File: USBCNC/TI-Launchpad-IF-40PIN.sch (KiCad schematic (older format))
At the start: 4 parts

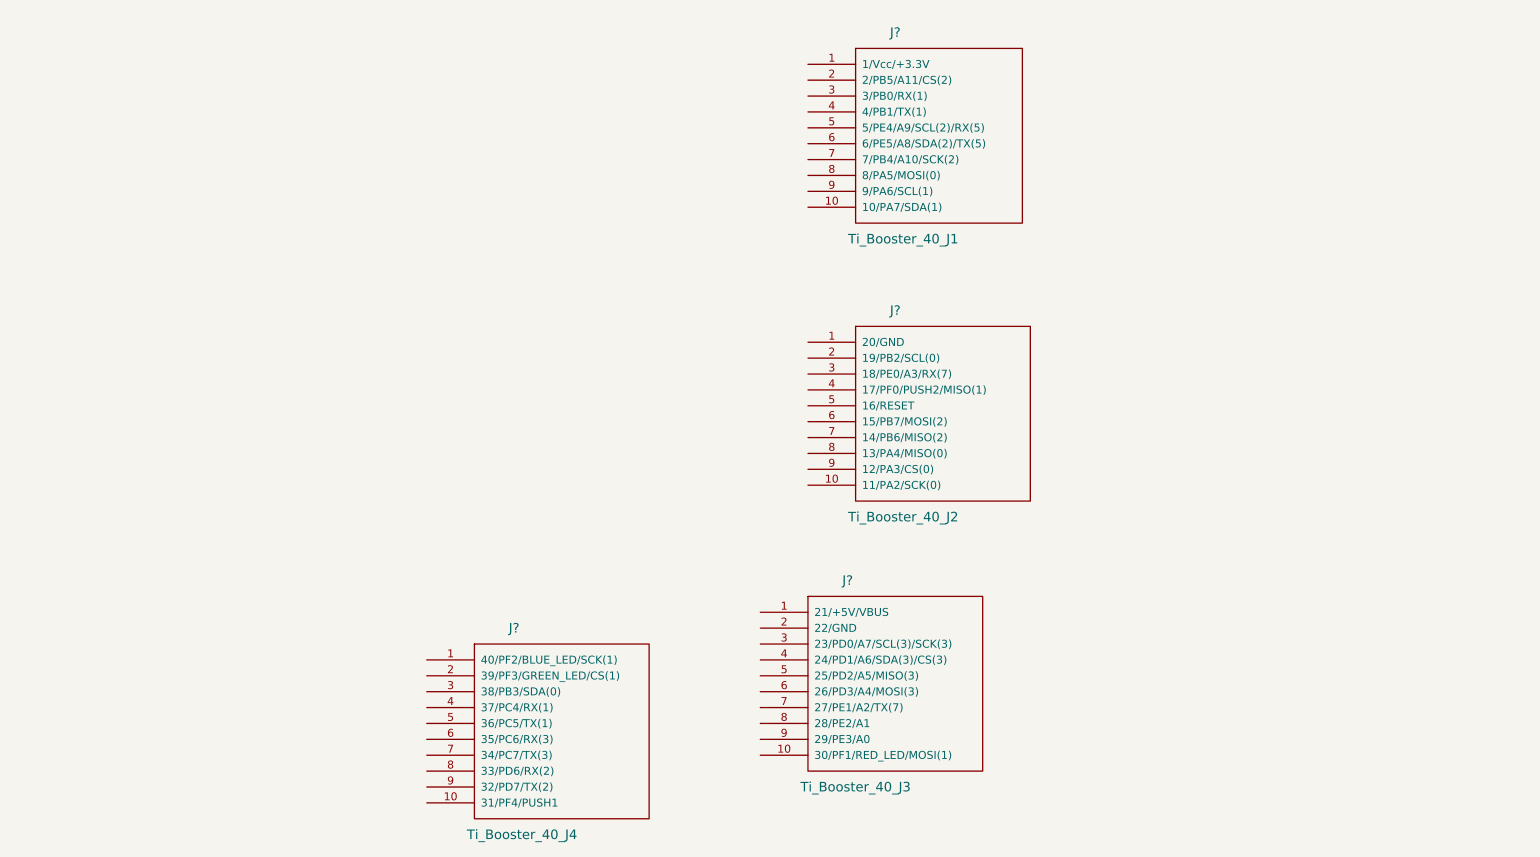
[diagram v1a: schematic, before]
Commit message: Specify global conections for the launchpad
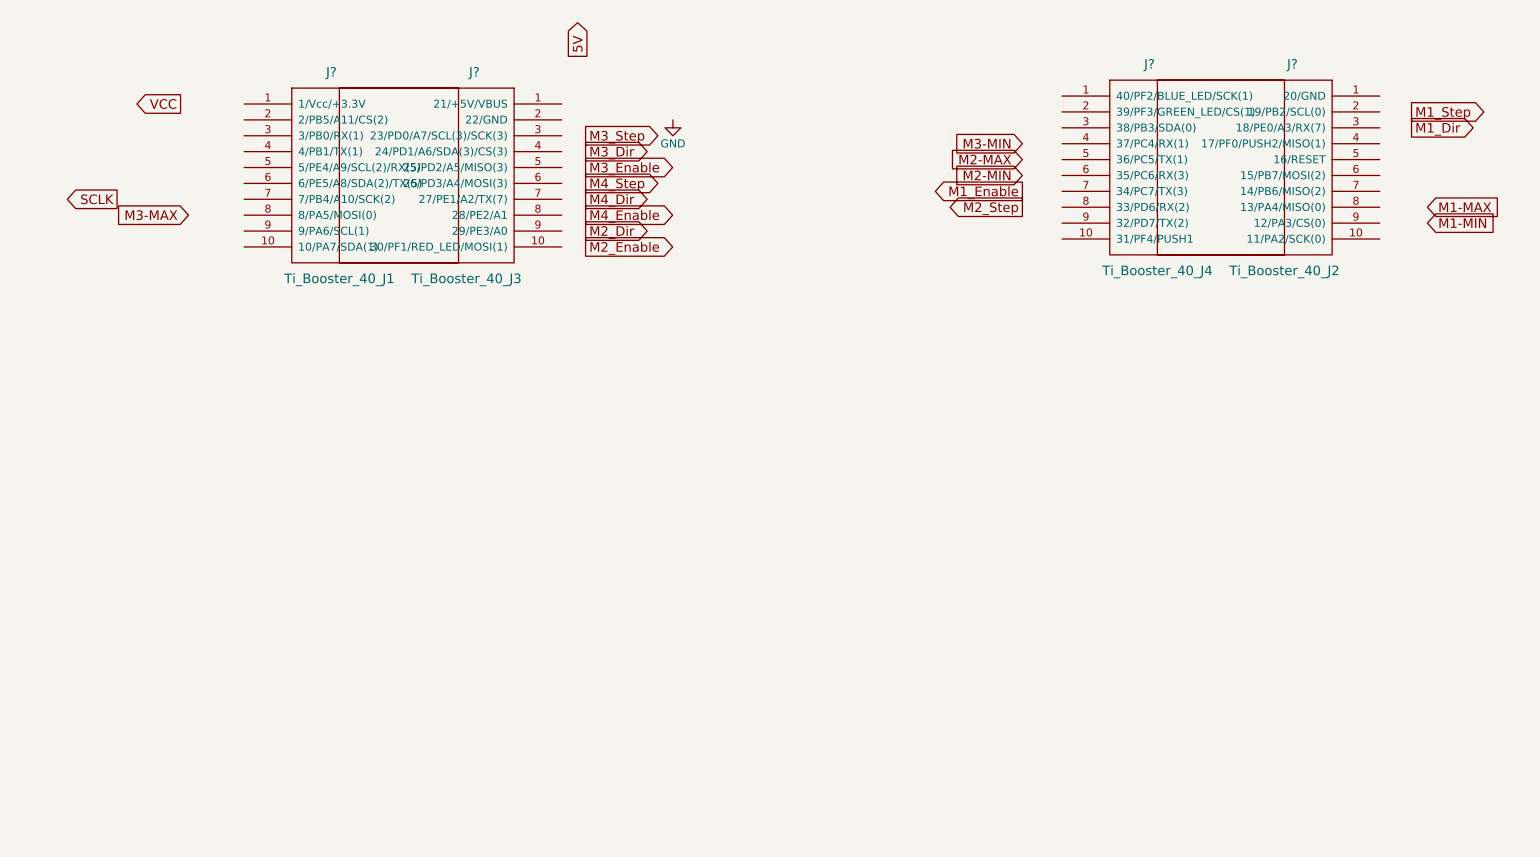
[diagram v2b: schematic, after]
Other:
- moved on the sheet: J?
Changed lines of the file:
@@
 L Ti_Booster_40_J1 J?
 U 1 1 559E3E8F
-P 6000 2500
-F 0 "J?" H 5950 3150 60  0000 C CNN
-F 1 "Ti_Booster_40_J1" H 6000 1850 60  0000 C CNN
-F 2 "" H 6000 2500 60  0000 C CNN
-F 3 "" H 6000 2500 60  0000 C CNN
-	1    6000 2500
+P 2450 2750
+F 0 "J?" H 2400 3400 60  0000 C CNN
+F 1 "Ti_Booster_40_J1" H 2450 2100 60  0000 C CNN
+F 2 "" H 2450 2750 60  0000 C CNN
+F 3 "" H 2450 2750 60  0000 C CNN
+	1    2450 2750
 	1    0    0    -1
 $EndComp
@@
 L Ti_Booster_40_J2 J?
 U 1 1 559E3EEE
-P 6000 4250
-F 0 "J?" H 5950 4900 60  0000 C CNN
-F 1 "Ti_Booster_40_J2" H 6000 3600 60  0000 C CNN
-F 2 "" H 6000 4250 60  0000 C CNN
-F 3 "" H 6000 4250 60  0000 C CNN
-	1    6000 4250
-	1    0    0    -1
+P 8400 2700
+F 0 "J?" H 8350 3350 60  0000 C CNN
+F 1 "Ti_Booster_40_J2" H 8400 2050 60  0000 C CNN
+F 2 "" H 8400 2700 60  0000 C CNN
+F 3 "" H 8400 2700 60  0000 C CNN
+	1    8400 2700
+	-1   0    0    -1
 $EndComp
 $Comp
 L Ti_Booster_40_J3 J?
 U 1 1 559E3F8D
-P 5700 5950
-F 0 "J?" H 5650 6600 60  0000 C CNN
-F 1 "Ti_Booster_40_J3" H 5700 5300 60  0000 C CNN
-F 2 "" H 5700 5950 60  0000 C CNN
-F 3 "" H 5700 5950 60  0000 C CNN
-	1    5700 5950
-	1    0    0    -1
+P 3250 2750
+F 0 "J?" H 3200 3400 60  0000 C CNN
+F 1 "Ti_Booster_40_J3" H 3250 2100 60  0000 C CNN
+F 2 "" H 3250 2750 60  0000 C CNN
+F 3 "" H 3250 2750 60  0000 C CNN
+	1    3250 2750
+	-1   0    0    -1
 $EndComp
 $Comp
 L Ti_Booster_40_J4 J?
 U 1 1 559E403A
-P 3600 6250
-F 0 "J?" H 3550 6900 60  0000 C CNN
-F 1 "Ti_Booster_40_J4" H 3600 5600 60  0000 C CNN
-F 2 "" H 3600 6250 60  0000 C CNN
-F 3 "" H 3600 6250 60  0000 C CNN
-	1    3600 6250
+P 7600 2700
+F 0 "J?" H 7550 3350 60  0000 C CNN
+F 1 "Ti_Booster_40_J4" H 7600 2050 60  0000 C CNN
+F 2 "" H 7600 2700 60  0000 C CNN
+F 3 "" H 7600 2700 60  0000 C CNN
+	1    7600 2700
 	1    0    0    -1
 $EndComp
+Text GLabel 1450 2300 0    60   Output ~ 0
+VCC
+Text GLabel 1050 2900 0    60   Output ~ 0
+SCLK
+Text GLabel 3950 2000 1    60   Output ~ 0
+5V
+$Comp
+L GND #PWR?
+U 1 1 55A2A931
+P 4550 2400
+F 0 "#PWR?" H 4550 2150 50  0001 C CNN
+F 1 "GND" H 4550 2250 50  0000 C CNN
+F 2 "" H 4550 2400 60  0000 C CNN
+F 3 "" H 4550 2400 60  0000 C CNN
+	1    4550 2400
+	1    0    0    -1
+$EndComp
+Text GLabel 4000 2500 2    60   Output ~ 0
+M3_Step
+Text GLabel 4000 2600 2    60   Output ~ 0
+M3_Dir
+Text GLabel 4000 2700 2    60   Output ~ 0
+M3_Enable
+Text GLabel 4000 2800 2    60   Output ~ 0
+M4_Step
+Text GLabel 4000 2900 2    60   Output ~ 0
+M4_Dir
+Text GLabel 4000 3000 2    60   Output ~ 0
+M4_Enable
+Text GLabel 6750 2950 0    60   Output ~ 0
+M2_Step
+Text GLabel 4000 3100 2    60   Output ~ 0
+M2_Dir
+Text GLabel 4000 3200 2    60   Output ~ 0
+M2_Enable
+Text GLabel 9200 2350 2    60   Output ~ 0
+M1_Step
+Text GLabel 9200 2450 2    60   Output ~ 0
+M1_Dir
+Text GLabel 6750 2850 0    60   Output ~ 0
+M1_Enable
+Text GLabel 9300 3050 2    60   Input ~ 0
+M1-MIN
+Text GLabel 9300 2950 2    60   Input ~ 0
+M1-MAX
+Text GLabel 6750 2750 0    60   Input ~ 0
+M2-MIN
+Text GLabel 6750 2650 0    60   Input ~ 0
+M2-MAX
+Text GLabel 6750 2550 0    60   Input ~ 0
+M3-MIN
+Text GLabel 1500 3000 0    60   Input ~ 0
+M3-MAX
 $EndSCHEMATC

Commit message: Added components for one  on board stepper driver
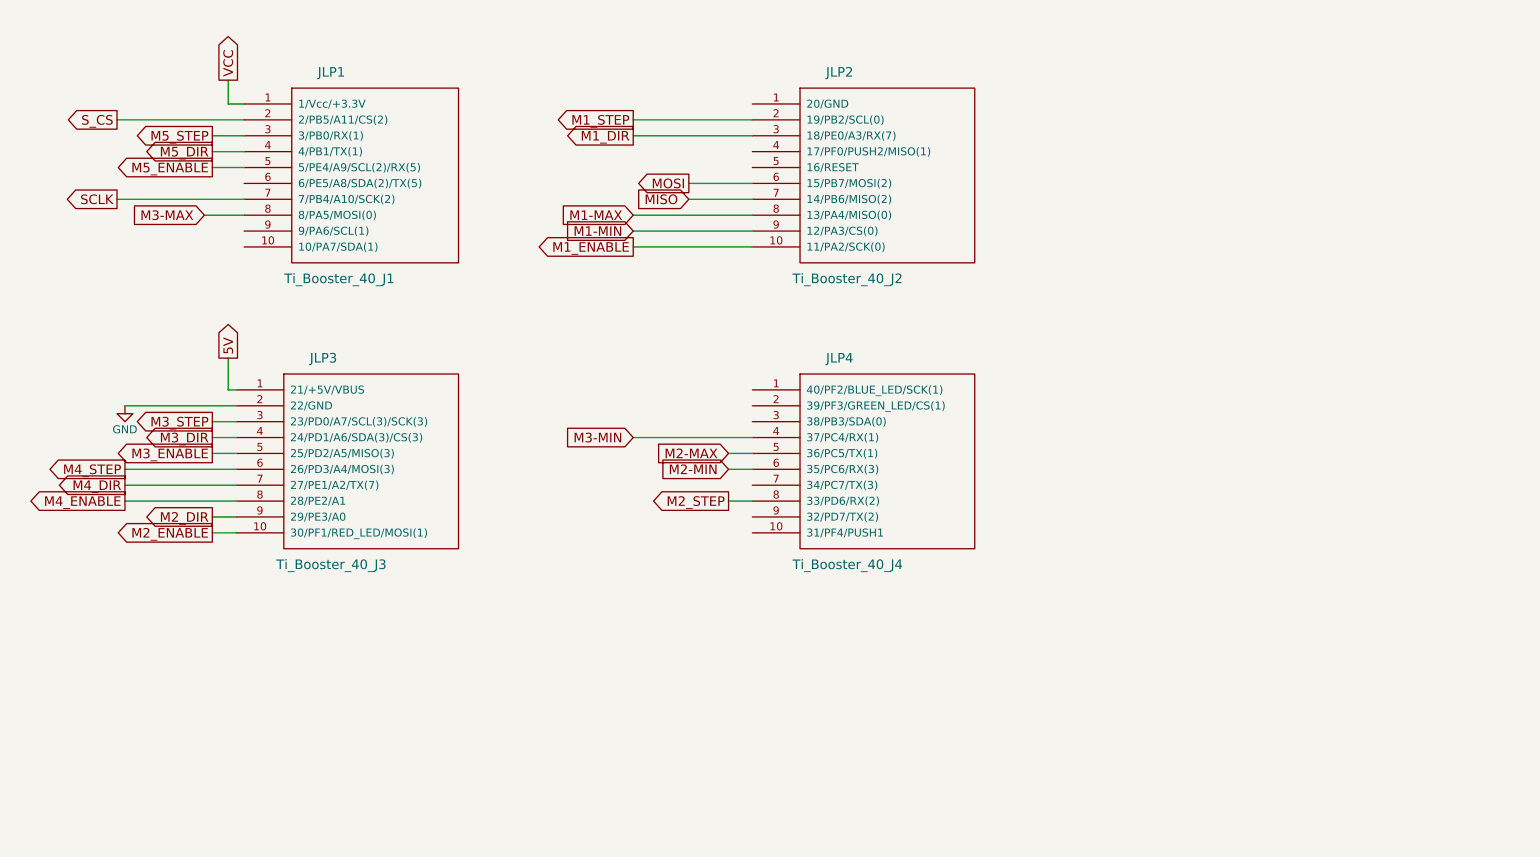
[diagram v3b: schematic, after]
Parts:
- gave numbers to parts that had none: 4
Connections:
- net 5V: now also JLP3.1 (21/+5V/VBUS)
- net GND: now also JLP3.2 (22/GND)
- net M1-MAX: now also JLP2.8 (13/PA4/MISO(0))
- net M1-MIN: now also JLP2.9 (12/PA3/CS(0))
- net M2-MAX: now also JLP4.5 (36/PC5/TX(1))
- net M2-MIN: now also JLP4.6 (35/PC6/RX(3))
- net M3-MAX: now also JLP1.8 (8/PA5/MOSI(0))
- net M3-MIN: now also JLP4.4 (37/PC4/RX(1))
- net SCLK: now also JLP1.7 (7/PB4/A10/SCK(2))
- net VCC: now also JLP1.1 (1/Vcc/+3.3V)
- net S_CS: now reaches JLP1.2 (2/PB5/A11/CS(2))
- net M5_STEP: now reaches JLP1.3 (3/PB0/RX(1))
- net M5_DIR: now reaches JLP1.4 (4/PB1/TX(1))
- net M5_ENABLE: now reaches JLP1.5 (5/PE4/A9/SCL(2)/RX(5))
- net M1_ENABLE: now reaches JLP2.10 (11/PA2/SCK(0))
- net M1_STEP: now reaches JLP2.2 (19/PB2/SCL(0))
- net M1_DIR: now reaches JLP2.3 (18/PE0/A3/RX(7))
- net MOSI: now reaches JLP2.6 (15/PB7/MOSI(2))
- net MISO: now reaches JLP2.7 (14/PB6/MISO(2))
- net M2_ENABLE: now reaches JLP3.10 (30/PF1/RED_LED/MOSI(1))
- net M3_STEP: now reaches JLP3.3 (23/PD0/A7/SCL(3)/SCK(3))
- net M3_DIR: now reaches JLP3.4 (24/PD1/A6/SDA(3)/CS(3))
- net M3_ENABLE: now reaches JLP3.5 (25/PD2/A5/MISO(3))
- net M4_STEP: now reaches JLP3.6 (26/PD3/A4/MOSI(3))
- net M4_DIR: now reaches JLP3.7 (27/PE1/A2/TX(7))
- net M4_ENABLE: now reaches JLP3.8 (28/PE2/A1)
- net M2_DIR: now reaches JLP3.9 (29/PE3/A0)
- net M2_STEP: now reaches JLP4.8 (33/PD6/RX(2))
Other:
- moved on the sheet: JLP2, JLP3, JLP4
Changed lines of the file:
@@
 $EndDescr
 $Comp
-L Ti_Booster_40_J1 J?
+L Ti_Booster_40_J1 JLP1
 U 1 1 559E3E8F
 P 2450 2750
-F 0 "J?" H 2400 3400 60  0000 C CNN
+F 0 "JLP1" H 2400 3400 60  0000 C CNN
 F 1 "Ti_Booster_40_J1" H 2450 2100 60  0000 C CNN
 F 2 "" H 2450 2750 60  0000 C CNN
@@
 $EndComp
 $Comp
-L Ti_Booster_40_J2 J?
+L Ti_Booster_40_J2 JLP2
 U 1 1 559E3EEE
-P 8400 2700
-F 0 "J?" H 8350 3350 60  0000 C CNN
-F 1 "Ti_Booster_40_J2" H 8400 2050 60  0000 C CNN
-F 2 "" H 8400 2700 60  0000 C CNN
-F 3 "" H 8400 2700 60  0000 C CNN
-	1    8400 2700
-	-1   0    0    -1
+P 5650 2750
+F 0 "JLP2" H 5600 3400 60  0000 C CNN
+F 1 "Ti_Booster_40_J2" H 5650 2100 60  0000 C CNN
+F 2 "" H 5650 2750 60  0000 C CNN
+F 3 "" H 5650 2750 60  0000 C CNN
+	1    5650 2750
+	1    0    0    -1
 $EndComp
 $Comp
-L Ti_Booster_40_J3 J?
+L Ti_Booster_40_J3 JLP3
 U 1 1 559E3F8D
-P 3250 2750
-F 0 "J?" H 3200 3400 60  0000 C CNN
-F 1 "Ti_Booster_40_J3" H 3250 2100 60  0000 C CNN
-F 2 "" H 3250 2750 60  0000 C CNN
-F 3 "" H 3250 2750 60  0000 C CNN
-	1    3250 2750
-	-1   0    0    -1
+P 2400 4550
+F 0 "JLP3" H 2350 5200 60  0000 C CNN
+F 1 "Ti_Booster_40_J3" H 2400 3900 60  0000 C CNN
+F 2 "" H 2400 4550 60  0000 C CNN
+F 3 "" H 2400 4550 60  0000 C CNN
+	1    2400 4550
+	1    0    0    -1
 $EndComp
 $Comp
-L Ti_Booster_40_J4 J?
+L Ti_Booster_40_J4 JLP4
 U 1 1 559E403A
-P 7600 2700
-F 0 "J?" H 7550 3350 60  0000 C CNN
-F 1 "Ti_Booster_40_J4" H 7600 2050 60  0000 C CNN
-F 2 "" H 7600 2700 60  0000 C CNN
-F 3 "" H 7600 2700 60  0000 C CNN
-	1    7600 2700
+P 5650 4550
+F 0 "JLP4" H 5600 5200 60  0000 C CNN
+F 1 "Ti_Booster_40_J4" H 5650 3900 60  0000 C CNN
+F 2 "" H 5650 4550 60  0000 C CNN
+F 3 "" H 5650 4550 60  0000 C CNN
+	1    5650 4550
 	1    0    0    -1
 $EndComp
-Text GLabel 1450 2300 0    60   Output ~ 0
+Text GLabel 1750 2150 1    60   Output ~ 0
 VCC
 Text GLabel 1050 2900 0    60   Output ~ 0
 SCLK
-Text GLabel 3950 2000 1    60   Output ~ 0
+Text GLabel 1750 3900 1    60   Output ~ 0
 5V
 $Comp
 L GND #PWR?
 U 1 1 55A2A931
-P 4550 2400
-F 0 "#PWR?" H 4550 2150 50  0001 C CNN
-F 1 "GND" H 4550 2250 50  0000 C CNN
-F 2 "" H 4550 2400 60  0000 C CNN
-F 3 "" H 4550 2400 60  0000 C CNN
-	1    4550 2400
-	1    0    0    -1
+P 1100 4200
+F 0 "#PWR?" H 1100 3950 50  0001 C CNN
+F 1 "GND" H 1100 4050 50  0000 C CNN
+F 2 "" H 1100 4200 60  0000 C CNN
+F 3 "" H 1100 4200 60  0000 C CNN
+	1    1100 4200
+	-1   0    0    -1
 $EndComp
-Text GLabel 4000 2500 2    60   Output ~ 0
-M3_Step
-Text GLabel 4000 2600 2    60   Output ~ 0
-M3_Dir
-Text GLabel 4000 2700 2    60   Output ~ 0
-M3_Enable
-Text GLabel 4000 2800 2    60   Output ~ 0
-M4_Step
-Text GLabel 4000 2900 2    60   Output ~ 0
-M4_Dir
-Text GLabel 4000 3000 2    60   Output ~ 0
-M4_Enable
-Text GLabel 6750 2950 0    60   Output ~ 0
-M2_Step
-Text GLabel 4000 3100 2    60   Output ~ 0
-M2_Dir
-Text GLabel 4000 3200 2    60   Output ~ 0
-M2_Enable
-Text GLabel 9200 2350 2    60   Output ~ 0
-M1_Step
-Text GLabel 9200 2450 2    60   Output ~ 0
-M1_Dir
-Text GLabel 6750 2850 0    60   Output ~ 0
-M1_Enable
-Text GLabel 9300 3050 2    60   Input ~ 0
+Text GLabel 1650 4300 0    60   Output ~ 0
+M3_STEP
+Text GLabel 1650 4400 0    60   Output ~ 0
+M3_DIR
+Text GLabel 1650 4500 0    60   Output ~ 0
+M3_ENABLE
+Text GLabel 1100 4600 0    60   Output ~ 0
+M4_STEP
+Text GLabel 1100 4700 0    60   Output ~ 0
+M4_DIR
+Text GLabel 1100 4800 0    60   Output ~ 0
+M4_ENABLE
+Text GLabel 4900 4800 0    60   Output ~ 0
+M2_STEP
+Text GLabel 1650 4900 0    60   Output ~ 0
+M2_DIR
+Text GLabel 1650 5000 0    60   Output ~ 0
+M2_ENABLE
+Text GLabel 4300 2400 0    60   Output ~ 0
+M1_STEP
+Text GLabel 4300 2500 0    60   Output ~ 0
+M1_DIR
+Text GLabel 4300 3200 0    60   Output ~ 0
+M1_ENABLE
+Text GLabel 4300 3100 0    60   Input ~ 0
 M1-MIN
-Text GLabel 9300 2950 2    60   Input ~ 0
+Text GLabel 4300 3000 0    60   Input ~ 0
 M1-MAX
-Text GLabel 6750 2750 0    60   Input ~ 0
+Text GLabel 4900 4600 0    60   Input ~ 0
 M2-MIN
-Text GLabel 6750 2650 0    60   Input ~ 0
+Text GLabel 4900 4500 0    60   Input ~ 0
 M2-MAX
-Text GLabel 6750 2550 0    60   Input ~ 0
+Text GLabel 4300 4400 0    60   Input ~ 0
 M3-MIN
-Text GLabel 1500 3000 0    60   Input ~ 0
+Text GLabel 1600 3000 0    60   Input ~ 0
 M3-MAX
+Wire Wire Line
+	1850 2900 1050 2900
+Wire Wire Line
+	1850 3000 1600 3000
+Wire Wire Line
+	1800 4200 1100 4200
+Wire Wire Line
+	1750 4100 1750 3900
+Wire Wire Line
+	1650 4300 1800 4300
+Wire Wire Line
+	1800 4400 1650 4400
+Wire Wire Line
+	1800 4500 1650 4500
+Wire Wire Line
+	1800 4600 1100 4600
+Wire Wire Line
+	1100 4700 1800 4700
+Wire Wire Line
+	1800 4800 1100 4800
+Wire Wire Line
+	1650 4900 1800 4900
+Wire Wire Line
+	1800 5000 1650 5000
+Wire Wire Line
+	4300 4400 5050 4400
+Wire Wire Line
+	5050 4500 4900 4500
+Wire Wire Line
+	4900 4600 5050 4600
+Wire Wire Line
+	4900 4800 5050 4800
+Wire Wire Line
+	5050 3100 4300 3100
+Wire Wire Line
+	4300 3000 5050 3000
+Wire Wire Line
+	4300 2500 5050 2500
+Wire Wire Line
+	5050 2400 4300 2400
+Text GLabel 1050 2400 0    60   Output ~ 0
+S_CS
+Wire Wire Line
+	1850 2300 1750 2300
+Wire Wire Line
+	1750 2300 1750 2150
+Wire Wire Line
+	1850 2400 1050 2400
+Text GLabel 4650 2800 0    60   Output ~ 0
+MOSI
+Text GLabel 4650 2900 0    60   Input ~ 0
+MISO
+Wire Wire Line
+	5050 2900 4650 2900
+Wire Wire Line
+	4650 2800 5050 2800
+Text GLabel 1650 2500 0    60   Output ~ 0
+M5_STEP
+Text GLabel 1650 2600 0    60   Output ~ 0
+M5_DIR
+Text GLabel 1650 2700 0    60   Output ~ 0
+M5_ENABLE
+Wire Wire Line
+	1850 2500 1650 2500
+Wire Wire Line
+	1850 2600 1650 2600
+Wire Wire Line
+	1850 2700 1650 2700
+Wire Wire Line
+	5050 3200 4300 3200
+Wire Wire Line
+	1800 4100 1750 4100
 $EndSCHEMATC

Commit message: Completed the DRV8825 Block(s), and reorganized the pololu blocks
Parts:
- JLP1: symbol Ti_Booster_40_J1 -> Ti_Booster_40_J1-RESCUE-USBCNC
- JLP2: symbol Ti_Booster_40_J2 -> Ti_Booster_40_J2-RESCUE-USBCNC
- JLP3: symbol Ti_Booster_40_J3 -> Ti_Booster_40_J3-RESCUE-USBCNC
- JLP4: symbol Ti_Booster_40_J4 -> Ti_Booster_40_J4-RESCUE-USBCNC
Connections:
- net M2_STEP: now also JLP4.7 (34/PC7/TX(3)); no longer JLP4.8 (33/PD6/RX(2))
- net SDA: now reaches JLP1.10 (10/PA7/SDA(1))
- net SCL: now reaches JLP1.9 (9/PA6/SCL(1))
- net S_CS renamed ~SS
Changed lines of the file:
@@
 EESchema Schematic File Version 2
+LIBS:USBCNC-rescue
 LIBS:power
 LIBS:device
@@
 $EndDescr
 $Comp
-L Ti_Booster_40_J1 JLP1
+L Ti_Booster_40_J1-RESCUE-USBCNC JLP1
 U 1 1 559E3E8F
 P 2450 2750
+AR Path="/559E3E8F" Ref="JLP1"  Part="1"
+AR Path="/559E3E7E/559E3E8F" Ref="JLP1"  Part="1"
 F 0 "JLP1" H 2400 3400 60  0000 C CNN
 F 1 "Ti_Booster_40_J1" H 2450 2100 60  0000 C CNN
@@
 $EndComp
 $Comp
-L Ti_Booster_40_J2 JLP2
+L Ti_Booster_40_J2-RESCUE-USBCNC JLP2
 U 1 1 559E3EEE
 P 5650 2750
@@
 $EndComp
 $Comp
-L Ti_Booster_40_J3 JLP3
+L Ti_Booster_40_J3-RESCUE-USBCNC JLP3
 U 1 1 559E3F8D
 P 2400 4550
@@
 $EndComp
 $Comp
-L Ti_Booster_40_J4 JLP4
+L Ti_Booster_40_J4-RESCUE-USBCNC JLP4
 U 1 1 559E403A
 P 5650 4550
@@
 Text GLabel 1100 4800 0    60   Output ~ 0
 M4_ENABLE
-Text GLabel 4900 4800 0    60   Output ~ 0
+Text GLabel 4900 4700 0    60   Output ~ 0
 M2_STEP
 Text GLabel 1650 4900 0    60   Output ~ 0
@@
 Text GLabel 4900 4500 0    60   Input ~ 0
 M2-MAX
-Text GLabel 4300 4400 0    60   Input ~ 0
+Text GLabel 4350 4400 0    60   Input ~ 0
 M3-MIN
 Text GLabel 1600 3000 0    60   Input ~ 0
@@
 	1800 5000 1650 5000
 Wire Wire Line
-	4300 4400 5050 4400
-Wire Wire Line
 	5050 4500 4900 4500
 Wire Wire Line
 	4900 4600 5050 4600
-Wire Wire Line
-	4900 4800 5050 4800
 Wire Wire Line
 	5050 3100 4300 3100
@@
 	5050 2400 4300 2400
 Text GLabel 1050 2400 0    60   Output ~ 0
-S_CS
+~SS
 Wire Wire Line
 	1850 2300 1750 2300
@@
 Wire Wire Line
 	1800 4100 1750 4100
+Text GLabel 1050 3100 0    60   BiDi ~ 0
+SCL
+Text GLabel 1050 3200 0    60   BiDi ~ 0
+SDA
+Wire Wire Line
+	1850 3100 1050 3100
+Wire Wire Line
+	1050 3200 1850 3200
+Wire Wire Line
+	5050 4400 4350 4400
+Wire Wire Line
+	5050 4700 4900 4700
+Text GLabel 4400 4900 0    60   Output ~ 0
+UART_TX
+Text GLabel 4400 4800 0    60   Input ~ 0
+UART_RX
 $EndSCHEMATC
